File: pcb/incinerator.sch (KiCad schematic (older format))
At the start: 39 parts, among them J1 IGNITION1, J10 MAX31855 Breakout Board, J2 IGNITION2, J3 VALVE1, J4 VALVE2, J5 VALVE3, J6 AIRPMP, J7 Power Source 12V, J8 Waveshare 4.2\" e-paper, J9 MAX31855 Breakout Board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

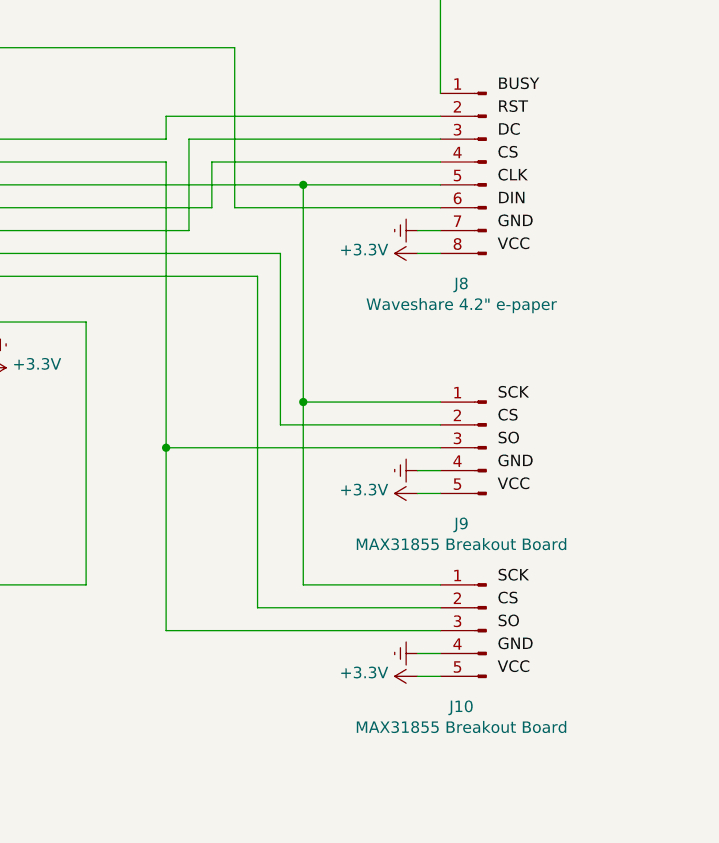
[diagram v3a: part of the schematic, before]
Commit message: Added KiCad symbol for thermocouple breakout board
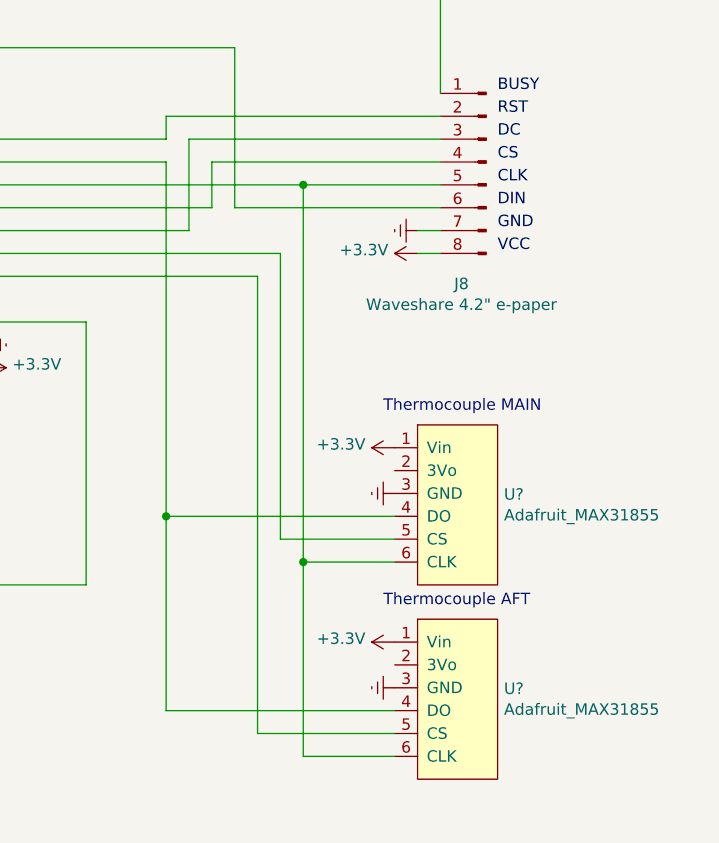
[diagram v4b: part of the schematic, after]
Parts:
- removed J10, J9: MAX31855 Breakout Board, symbol Connector:Conn_01x05_Male
- added U? (x2): Adafruit_MAX31855, symbol incinerator:Adafruit_MAX31855
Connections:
- net +3V3: now also U?.1 (Vin), U?.1 (Vin)
- net Earth: now also U?.3 (GND), U?.3 (GND)
- net at J8.5 (Pin_5), U2.24 (D18): now also U?.6 (CLK), U?.6 (CLK)
- net at U2.21 (RX2): now also U?.5 (CS)
- net at U2.25 (D19): now also U?.4 (DO), U?.4 (DO)
- net at U2.20 (D4): now also U?.5 (CS)
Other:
- note added: "Thermocouple AFT"
- note added: "Thermocouple MAIN"
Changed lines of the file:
@@
 Wire Wire Line
 	6900 5700 5900 5700
-Text Label 10400 5100 0    50   ~ 0
-VCC
-Text Label 10400 5000 0    50   ~ 0
-GND
-Text Label 10400 4900 0    50   ~ 0
-SO
-Text Label 10400 4800 0    50   ~ 0
-CS
-Text Label 10400 4700 0    50   ~ 0
-SCK
-$Comp
-L Connector:Conn_01x05_Male J9
-U 1 1 5DE8FF2A
-P 10350 4900
-F 0 "J9" H 10458 4567 50  0000 C CNN
-F 1 "MAX31855 Breakout Board" H 10458 4476 50  0000 C CNN
-F 2 "" H 10350 4900 50  0001 C CNN
-F 3 "~" H 10350 4900 50  0001 C CNN
-	1    10350 4900
-	-1   0    0    -1
-$EndComp
-Text Label 10400 5900 0    50   ~ 0
-VCC
-Text Label 10400 5800 0    50   ~ 0
-GND
-Text Label 10400 5700 0    50   ~ 0
-SO
-Text Label 10400 5600 0    50   ~ 0
-CS
-Text Label 10400 5500 0    50   ~ 0
-SCK
-$Comp
-L Connector:Conn_01x05_Male J10
-U 1 1 5DEAED10
-P 10350 5700
-F 0 "J10" H 10458 5367 50  0000 C CNN
-F 1 "MAX31855 Breakout Board" H 10458 5276 50  0000 C CNN
-F 2 "" H 10350 5700 50  0001 C CNN
-F 3 "~" H 10350 5700 50  0001 C CNN
-	1    10350 5700
-	-1   0    0    -1
-$EndComp
-Wire Wire Line
-	9550 3750 9550 4700
-Wire Wire Line
-	9550 4700 10150 4700
 Connection ~ 9550 3750
 Wire Wire Line
-	9550 4700 9550 5500
-Wire Wire Line
-	9550 5500 10150 5500
-Connection ~ 9550 4700
-Wire Wire Line
-	9450 4800 10150 4800
-Wire Wire Line
-	9450 4050 9450 4800
-Wire Wire Line
-	9350 4150 9350 5600
-Wire Wire Line
-	9350 5600 10150 5600
-Wire Wire Line
 	9250 3150 9250 3850
-Wire Wire Line
-	8950 3650 8950 4900
-Wire Wire Line
-	8950 4900 10150 4900
-Wire Wire Line
-	8950 4900 8950 5700
-Wire Wire Line
-	8950 5700 10150 5700
-Connection ~ 8950 4900
 Wire Wire Line
 	9550 3750 10150 3750
@@
 L power:Earth #PWR022
 U 1 1 5DF0E96B
-P 10050 5000
-F 0 "#PWR022" H 10050 4750 50  0001 C CNN
-F 1 "Earth" H 10050 4850 50  0001 C CNN
-F 2 "" H 10050 5000 50  0001 C CNN
-F 3 "~" H 10050 5000 50  0001 C CNN
-	1    10050 5000
+P 9950 5100
+F 0 "#PWR022" H 9950 4850 50  0001 C CNN
+F 1 "Earth" H 9950 4950 50  0001 C CNN
+F 2 "" H 9950 5100 50  0001 C CNN
+F 3 "~" H 9950 5100 50  0001 C CNN
+	1    9950 5100
 	0    1    1    0
 $EndComp
-Wire Wire Line
-	10050 5000 10150 5000
 $Comp
 L power:+3.3V #PWR023
 U 1 1 5DF0E972
-P 10050 5100
-F 0 "#PWR023" H 10050 4950 50  0001 C CNN
-F 1 "+3.3V" V 10065 5228 50  0000 L CNN
-F 2 "" H 10050 5100 50  0001 C CNN
-F 3 "" H 10050 5100 50  0001 C CNN
-	1    10050 5100
+P 9950 4900
+F 0 "#PWR023" H 9950 4750 50  0001 C CNN
+F 1 "+3.3V" V 9965 5028 50  0000 L CNN
+F 2 "" H 9950 4900 50  0001 C CNN
+F 3 "" H 9950 4900 50  0001 C CNN
+	1    9950 4900
 	0    -1   -1   0
 $EndComp
-Wire Wire Line
-	10050 5100 10150 5100
 $Comp
 L power:Earth #PWR024
 U 1 1 5DF11219
-P 10050 5800
-F 0 "#PWR024" H 10050 5550 50  0001 C CNN
-F 1 "Earth" H 10050 5650 50  0001 C CNN
-F 2 "" H 10050 5800 50  0001 C CNN
-F 3 "~" H 10050 5800 50  0001 C CNN
-	1    10050 5800
+P 9950 5950
+F 0 "#PWR024" H 9950 5700 50  0001 C CNN
+F 1 "Earth" H 9950 5800 50  0001 C CNN
+F 2 "" H 9950 5950 50  0001 C CNN
+F 3 "~" H 9950 5950 50  0001 C CNN
+	1    9950 5950
 	0    1    1    0
 $EndComp
-Wire Wire Line
-	10050 5800 10150 5800
 $Comp
 L power:+3.3V #PWR025
 U 1 1 5DF11220
-P 10050 5900
-F 0 "#PWR025" H 10050 5750 50  0001 C CNN
-F 1 "+3.3V" V 10065 6028 50  0000 L CNN
-F 2 "" H 10050 5900 50  0001 C CNN
-F 3 "" H 10050 5900 50  0001 C CNN
-	1    10050 5900
+P 9950 5750
+F 0 "#PWR025" H 9950 5600 50  0001 C CNN
+F 1 "+3.3V" V 9965 5878 50  0000 L CNN
+F 2 "" H 9950 5750 50  0001 C CNN
+F 3 "" H 9950 5750 50  0001 C CNN
+	1    9950 5750
 	0    -1   -1   0
 $EndComp
-Wire Wire Line
-	10050 5900 10150 5900
 Wire Wire Line
 	8600 4350 8600 5500
@@
 Wire Wire Line
 	7750 4550 8150 4550
+$Comp
+L incinerator:Adafruit_MAX31855 U?
+U 1 1 5E173AB4
+P 10200 6000
+F 0 "U?" H 10428 6046 50  0000 L CNN
+F 1 "Adafruit_MAX31855" H 10428 5955 50  0000 L CNN
+F 2 "" H 10250 5850 50  0001 C CNN
+F 3 "" H 10250 5850 50  0001 C CNN
+	1    10200 6000
+	1    0    0    -1
+$EndComp
+Wire Wire Line
+	9550 6250 9950 6250
+Wire Wire Line
+	9550 3750 9550 5400
+Wire Wire Line
+	9550 5400 9950 5400
+Connection ~ 9550 5400
+Wire Wire Line
+	9550 5400 9550 6250
+Wire Wire Line
+	8950 6050 9950 6050
+Wire Wire Line
+	8950 3650 8950 5200
+Wire Wire Line
+	9950 5200 8950 5200
+Connection ~ 8950 5200
+Wire Wire Line
+	8950 5200 8950 6050
+Wire Wire Line
+	9450 5300 9950 5300
+Wire Wire Line
+	9450 4050 9450 5300
+Wire Wire Line
+	9350 6150 9950 6150
+Wire Wire Line
+	9350 4150 9350 6150
+$Comp
+L incinerator:Adafruit_MAX31855 U?
+U 1 1 5E172B29
+P 10200 5150
+F 0 "U?" H 10428 5196 50  0000 L CNN
+F 1 "Adafruit_MAX31855" H 10428 5105 50  0000 L CNN
+F 2 "" H 10250 5000 50  0001 C CNN
+F 3 "" H 10250 5000 50  0001 C CNN
+	1    10200 5150
+	1    0    0    -1
+$EndComp
+Text Notes 9900 4750 0    50   ~ 0
+Thermocouple MAIN
+Text Notes 9900 5600 0    50   ~ 0
+Thermocouple AFT
 $EndSCHEMATC
